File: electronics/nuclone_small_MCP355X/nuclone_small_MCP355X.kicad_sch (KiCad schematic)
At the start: 86 parts, among them J1 Conn_01x04, J10 Conn_01x04, J11 Conn_01x04, J12 Conn_01x04, J13 Conn_01x04, J15 Conn_02x03_Odd_Even, J16 Conn_02x04_Odd_Even, J2 Conn_01x04, J3 nuclone_small_left, J4 nuclone_small_right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

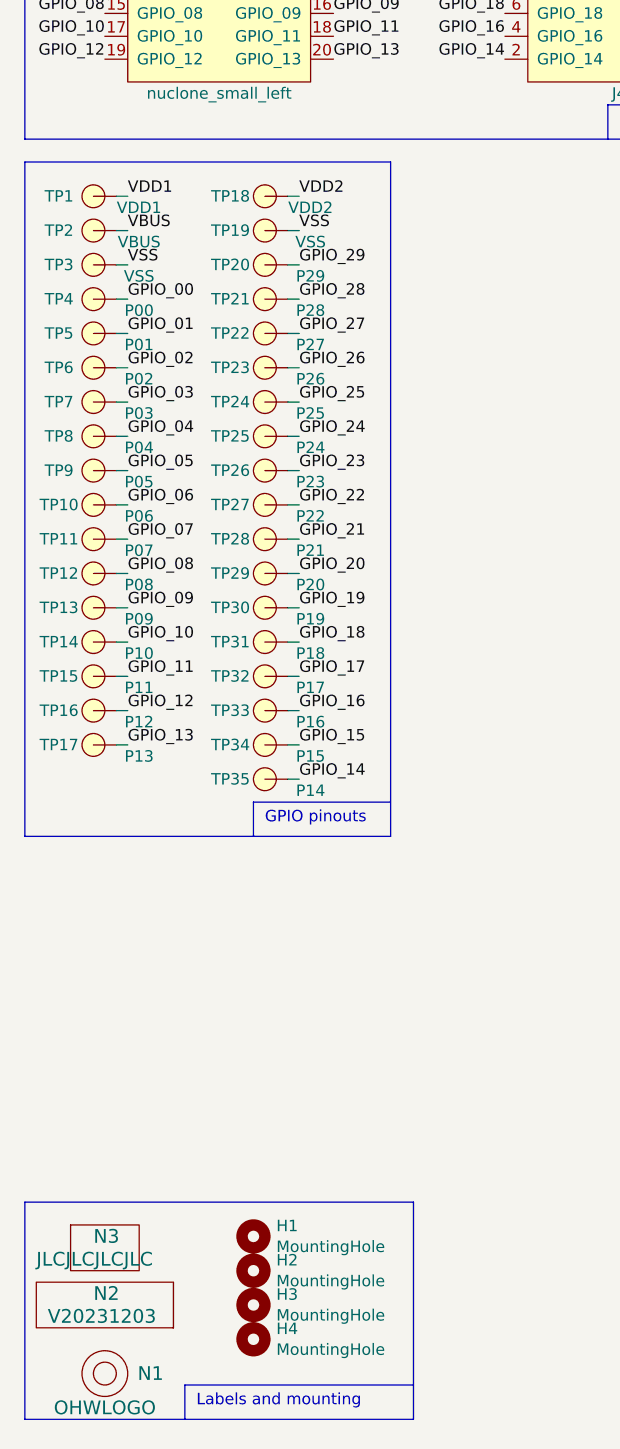
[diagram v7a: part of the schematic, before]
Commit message: applied aisler simple rules
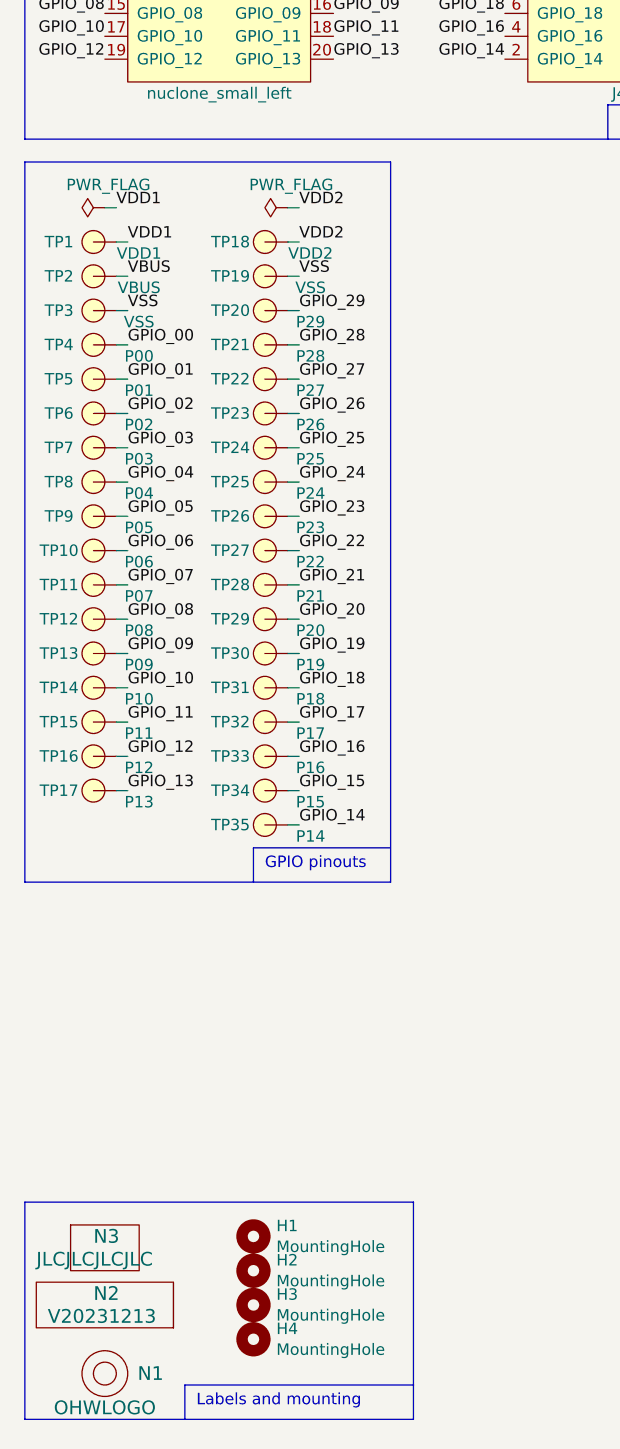
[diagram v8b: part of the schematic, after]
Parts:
- H1, H2, H3, H4: footprint MountingHole:MountingHole_3.2mm_M3_Pad_Via -> SquantorPcbOutline:MountingHole_3.2mm_M3_Pad_Via
- N2: value V20231203 -> V20231213
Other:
- moved on the sheet: TP1, TP10, TP11, TP12, TP13, TP14, TP15, TP16, TP17, TP18, TP19, TP2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
